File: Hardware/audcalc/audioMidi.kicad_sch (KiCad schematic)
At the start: 42 parts, among them J3 line_in, J4 headphone_out, J5 midi_in, J6 midi_out, U3 TLV320AIC3204, U4 WMM7037AT2_mic, U5 HCPL-0631, U9 ME6211C

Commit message: update schematic doc block
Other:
- company: TWR -> Jonathan Brodsky
- title: TDM -> Aud Calc
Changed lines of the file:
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@@
 	(paper "A4")
 	(title_block
-		(title "TDM")
-		(date "2021-09-17")
-		(rev "6")
-		(company "TWR")
-		(comment 1 "Pocket Sound Computer")
+		(title "Aud Calc")
+		(date "2024-04-04")
+		(rev "12")
+		(company "Jonathan Brodsky")
+		(comment 1 "Pocket Sound Calculator")
 	)
 	(junction

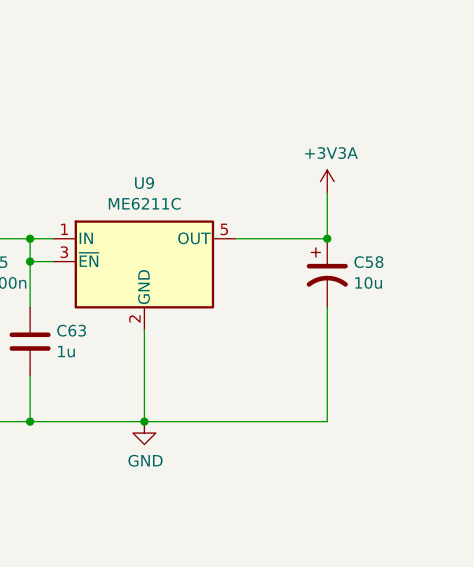
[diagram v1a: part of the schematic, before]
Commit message: fixed up bom for JLC
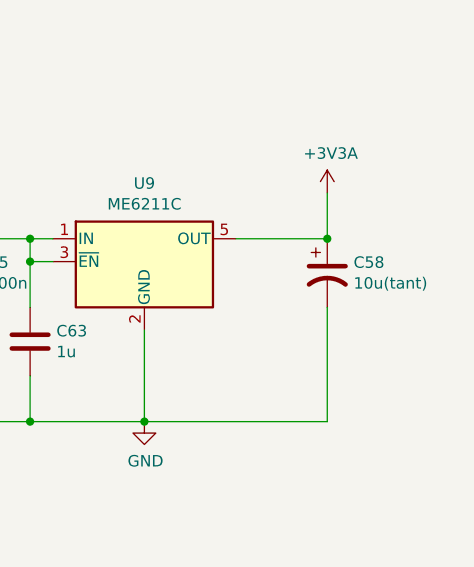
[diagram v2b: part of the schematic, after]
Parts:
- C58: value 10u -> 10u(tant)
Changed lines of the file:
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@@
 			)
 		)
-		(property "Value" "10u"
+		(property "Value" "10u(tant)"
 			(at 272.161 139.573 0)
 			(effects
